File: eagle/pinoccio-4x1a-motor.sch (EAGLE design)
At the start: 11 parts, among them IC1 74LVC1G04DBV, J1 POWER_JACKPTH, U1 TB6621FNG, U2 TB6621FNG

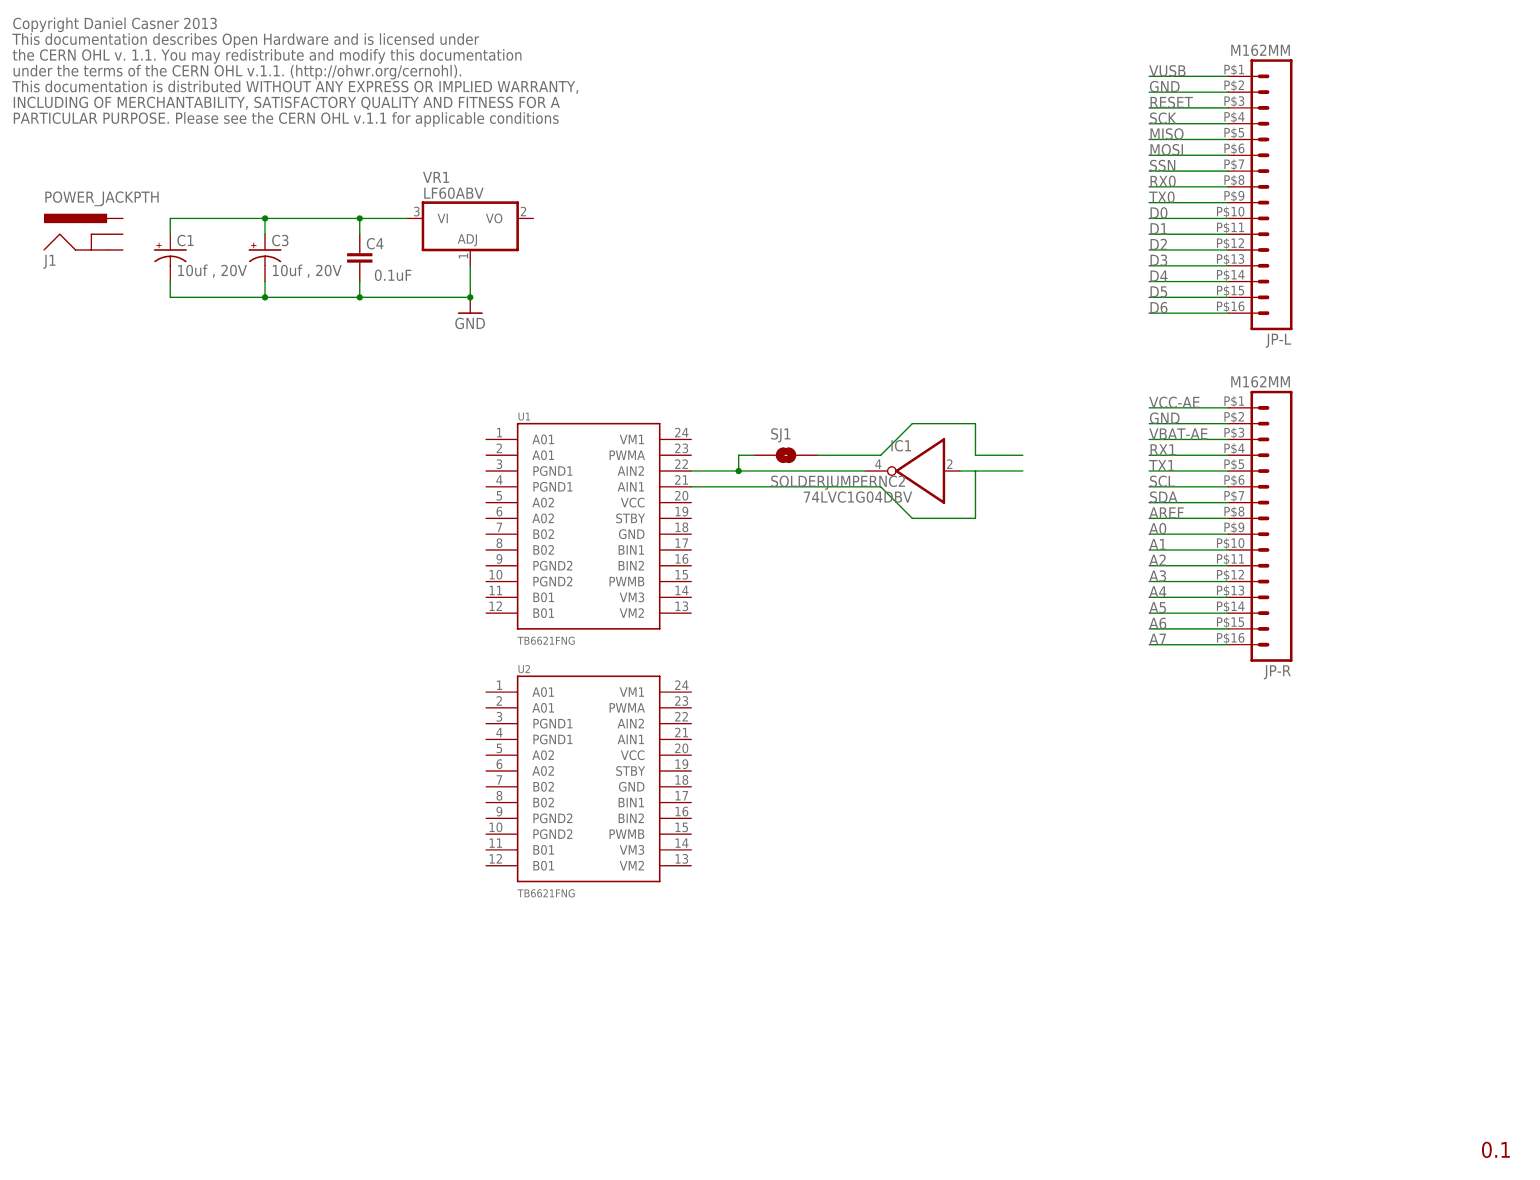
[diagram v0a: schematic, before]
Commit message: Finish first draft of schematic
Initial placement.
Add design rules file from OSHPark.com
Export PDFs of schematic and board.
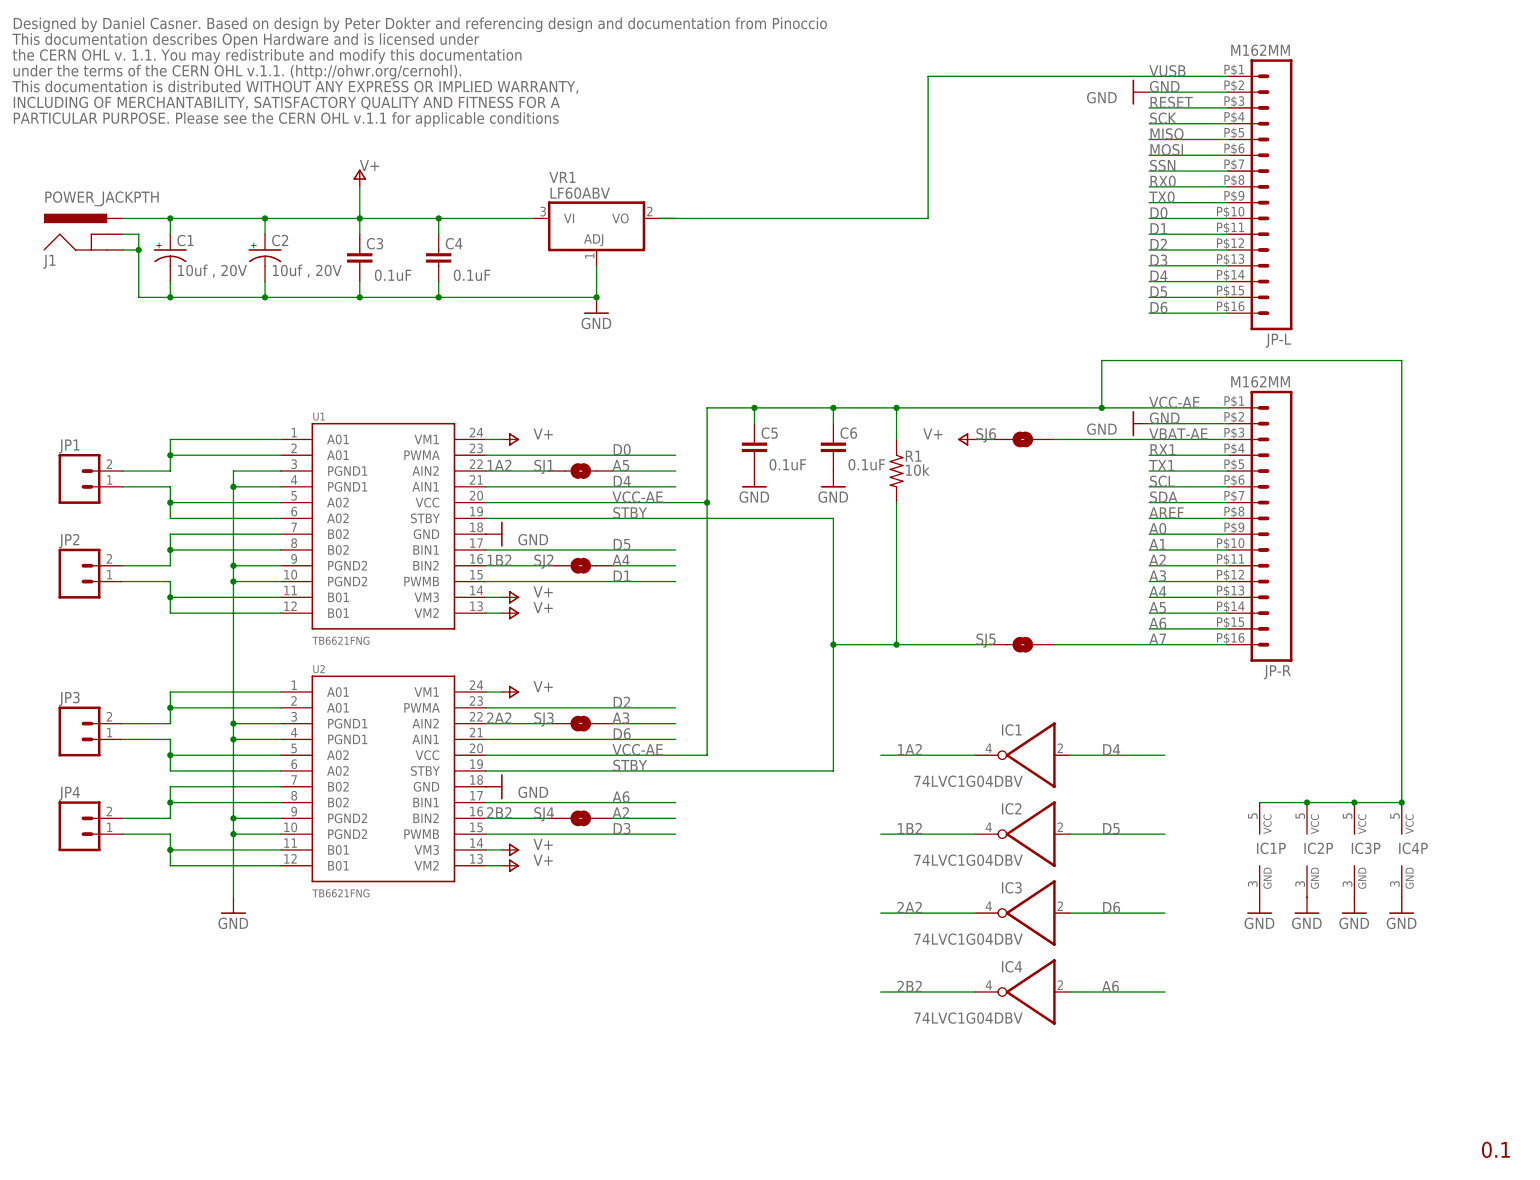
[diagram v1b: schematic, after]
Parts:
- added C2: 10uf , 20V, SparkFun:CAP_POL3528
- added C5, C6: 0.1uF, SparkFun:CAP0402-CAP
- added IC2, IC3, IC4: 74LVC1G04DBV, 74xx-little-de:74LVC1G04DBV
- added JP1, JP2, JP3, JP4: (no value), SparkFun-Connectors:M02LOCK_LONGPADS
- added R1: 10k, rcl:R-US_R0402
- added SJ2, SJ3, SJ4, SJ5, SJ6: SOLDERJUMPERNC2, SparkFun-Passives:SOLDERJUMPERNC2
- C3: value 10uf , 20V -> 0.1uF; device SparkFun:CAP_POL3528 -> SparkFun:CAP0402-CAP
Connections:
- net N$3 renamed 1A2
- removed net N$1: C1.+, C3.+, C4.2, VR1.VI
- removed net N$2: IC1A.I, U1.AIN1
- removed net N$4: SJ1.2
- new net 1B2: IC2A.O, SJ2.1, U1.BIN2
- new net 2A2: IC3A.O, SJ3.1, U2.AIN2
- new net 2B2: IC4A.O, SJ4.1, U2.BIN2
- new net M1+: JP1.2, U1.A01@1, U1.A01@2
- new net M1-: JP1.1, U1.A02@5, U1.A02@6
- new net M2+: JP2.2, U1.B02@7, U1.B02@8
- new net M2-: JP2.1, U1.B01@11, U1.B01@12
- new net M3+: JP3.2, U2.A01@1, U2.A01@2
- new net M3-: JP3.1, U2.A02@5, U2.A02@6
- new net M4+: JP4.2, U2.B02@7, U2.B02@8
- new net N$8: JP4.1, U2.B01@11, U2.B01@12
- new net STBY: R1.2, SJ5.1, U1.STBY, U2.STBY
- new net V+: C1.+, C2.+, C3.2, C4.2, J1.PWR, SJ6.1, U1.VM1, U1.VM2, U1.VM3, U2.VM1, U2.VM2, U2.VM3, VR1.VI
- net A2: now also SJ4.2
- net A3: now also SJ3.2
- net A4: now also SJ2.2
- net A5: now also SJ1.2
- net A6: now also IC4A.I, U2.BIN1
- net A7: now also SJ5.2
- net D0: now also U1.PWMA
- net D1: now also U1.PWMB
- net D2: now also U2.PWMA
- net D3: now also U2.PWMB
- net D4: now also IC1A.I, U1.AIN1
- net D5: now also IC2A.I, U1.BIN1
- net D6: now also IC3A.I, U2.AIN1
- net GND: now also C2.-, C3.1, C5.1, C6.1, IC1P.GND, IC2P.GND, IC3P.GND, IC4P.GND, J1.GND, J1.GNDBREAK, U1.GND, U1.PGND1@3, U1.PGND1@4, U1.PGND2@10, U1.PGND2@9, U2.GND, U2.PGND1@3, U2.PGND1@4, U2.PGND2@10, U2.PGND2@9; no longer C3.-
- net VBAT-AE: now also SJ6.2
- net VCC-AE: now also C5.2, C6.2, IC1P.VCC, IC2P.VCC, IC3P.VCC, IC4P.VCC, R1.1, U1.VCC, U2.VCC
- net VUSB: now also VR1.VO
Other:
- note added: "Designed by Daniel Casner. Based on design by Peter Dokter and referencing design and documentation from Pinoccio"
- note removed: "Copyright Daniel Casner 2013"
- moved on the sheet: C4, IC1, SJ1, U1, U2, VR1

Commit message: Working on manual routing.
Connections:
- net N$8 renamed M4-
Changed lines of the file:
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@@
 </segment>
 </net>
-<net name="N$8" class="0">
+<net name="M4-" class="0">
 <segment>
 <pinref part="U2" gate="G$1" pin="B01@11"/>

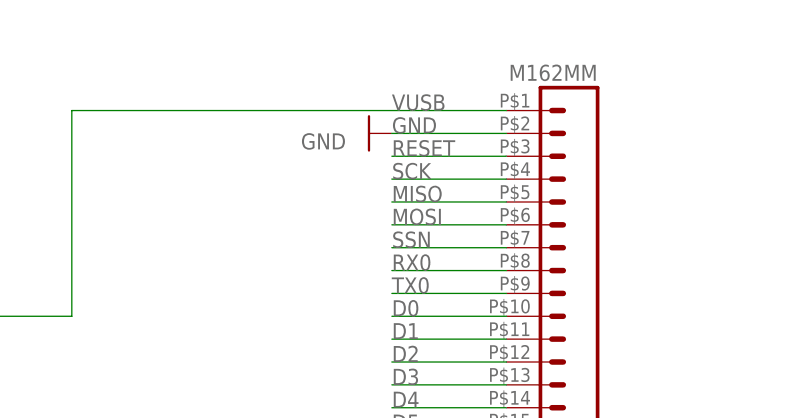
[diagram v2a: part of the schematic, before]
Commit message: A tiny bit more work. Putting everything on hold until the new backpack interface is documented.
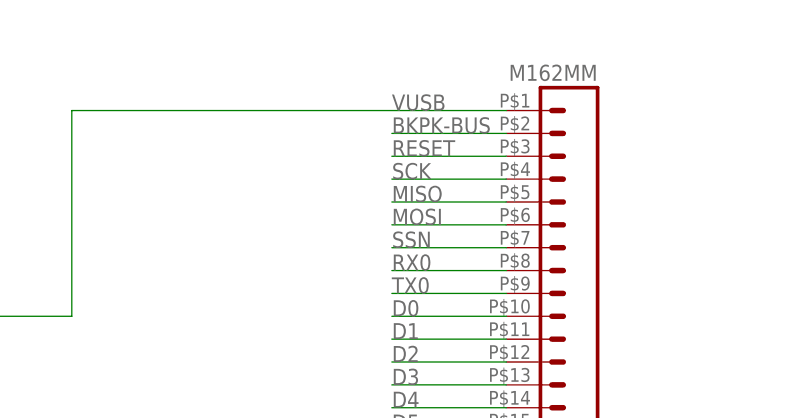
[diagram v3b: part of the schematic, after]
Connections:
- new net BKPK-BUS: JP-L.2
- net GND: no longer JP-L.2
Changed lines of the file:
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@@
 <part name="P+3" library="supply1" deviceset="V+" device=""/>
 <part name="P+4" library="supply1" deviceset="V+" device=""/>
-<part name="GND2" library="SparkFun-Aesthetics" deviceset="GND" device=""/>
 <part name="GND3" library="SparkFun-Aesthetics" deviceset="GND" device=""/>
 <part name="GND4" library="SparkFun-Aesthetics" deviceset="GND" device=""/>
@@
 <attribute name="VALUE" x="86.36" y="88.9" size="1.778" layer="96"/>
 </instance>
-<instance part="GND2" gate="1" x="182.88" y="172.72" smashed="yes" rot="R270">
-<attribute name="VALUE" x="180.34" y="172.72" size="1.778" layer="96" rot="R180"/>
-</instance>
 <instance part="GND3" gate="1" x="182.88" y="119.38" smashed="yes" rot="R270">
 <attribute name="VALUE" x="180.34" y="119.38" size="1.778" layer="96" rot="R180"/>
@@
 <net name="GND" class="5">
 <segment>
-<pinref part="JP-L" gate="G$1" pin="2"/>
-<label x="185.42" y="172.72" size="1.778" layer="95"/>
-<wire x1="198.12" y1="172.72" x2="185.42" y2="172.72" width="0.1524" layer="91"/>
-<pinref part="GND2" gate="1" pin="GND"/>
-</segment>
-<segment>
 <pinref part="JP-R" gate="G$1" pin="2"/>
 <wire x1="198.12" y1="119.38" x2="185.42" y2="119.38" width="0.1524" layer="91"/>
@@
 </segment>
 </net>
+<net name="BKPK-BUS" class="5">
+<segment>
+<pinref part="JP-L" gate="G$1" pin="2"/>
+<label x="185.42" y="172.72" size="1.778" layer="95"/>
+<wire x1="198.12" y1="172.72" x2="185.42" y2="172.72" width="0.1524" layer="91"/>
+</segment>
+</net>
